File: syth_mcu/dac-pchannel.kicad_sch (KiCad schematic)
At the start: 15 parts, among them J3 PJ-320A, U1 LM358

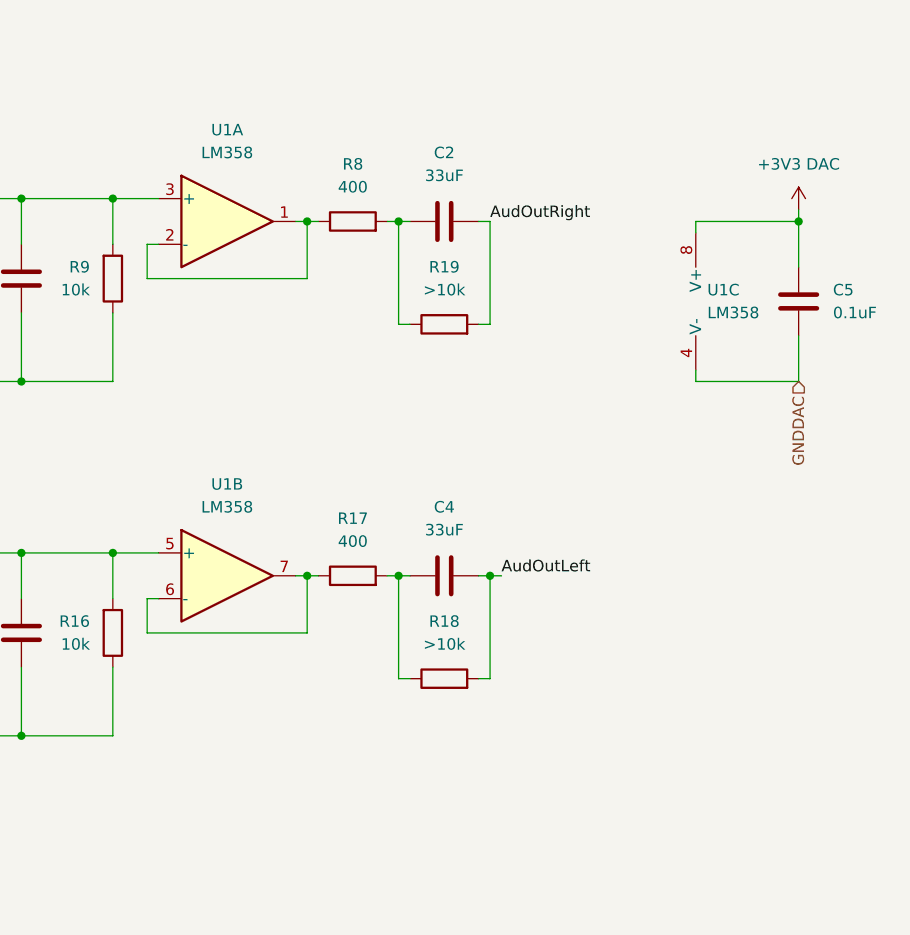
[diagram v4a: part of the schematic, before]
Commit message: v2 schematic merge, power and signal routing
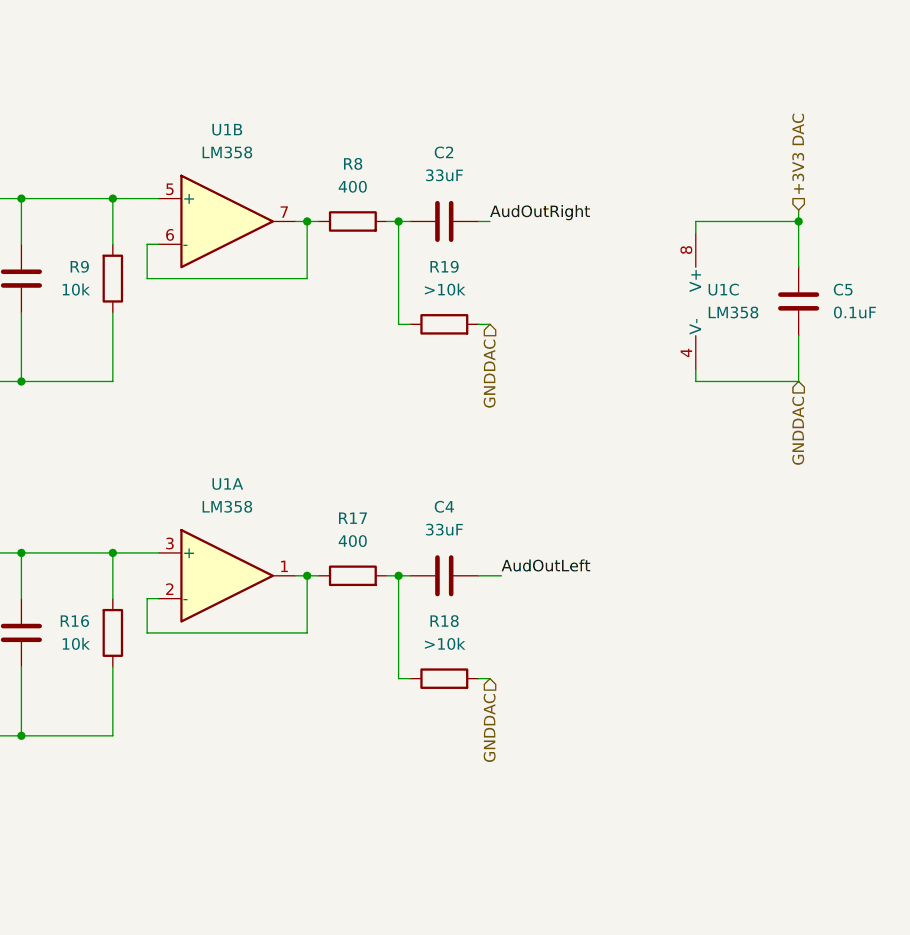
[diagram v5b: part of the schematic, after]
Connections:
- net AudOutLeft: no longer R18.2
- net AudOutRight: no longer R19.2
- net GNDDAC: now also R18.2, R19.2
- net at C3.1, R10.2, R16.2: now also U1.3 (+); no longer U1.5 (+)
- net at U1.1, U1.2 (-): now also R17.1; no longer R8.1
- net at C1.1, R7.2, R9.2: now also U1.5 (+); no longer U1.3 (+)
- net at U1.6 (-), U1.7: now also R8.1; no longer R17.1
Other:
- moved on the sheet: U1A, U1B
